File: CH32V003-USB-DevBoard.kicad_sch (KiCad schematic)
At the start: 23 parts, among them J1 USB_C_Receptacle_USB2.0, J2 Conn_01x10, J3 Conn_01x10, J4 Conn_01x01, SW1 SW_Push, U1 ME6211A33M3G-N, U3 CH32V003F4U6, Y1 24MHz

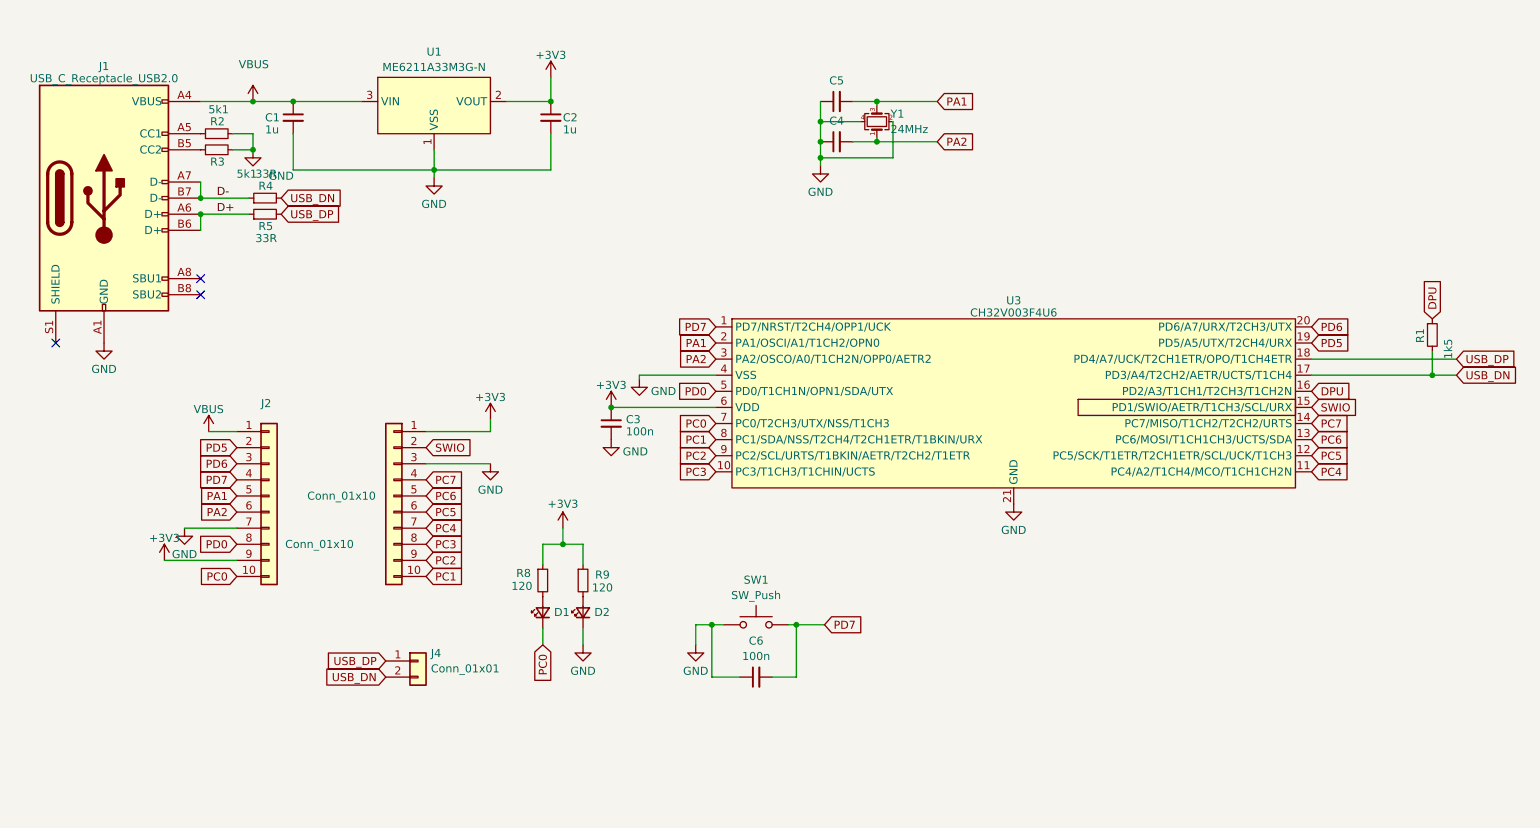
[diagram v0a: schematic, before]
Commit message: Make design easier to hand solder Switch to ch340n instead of S/W bit banged USB
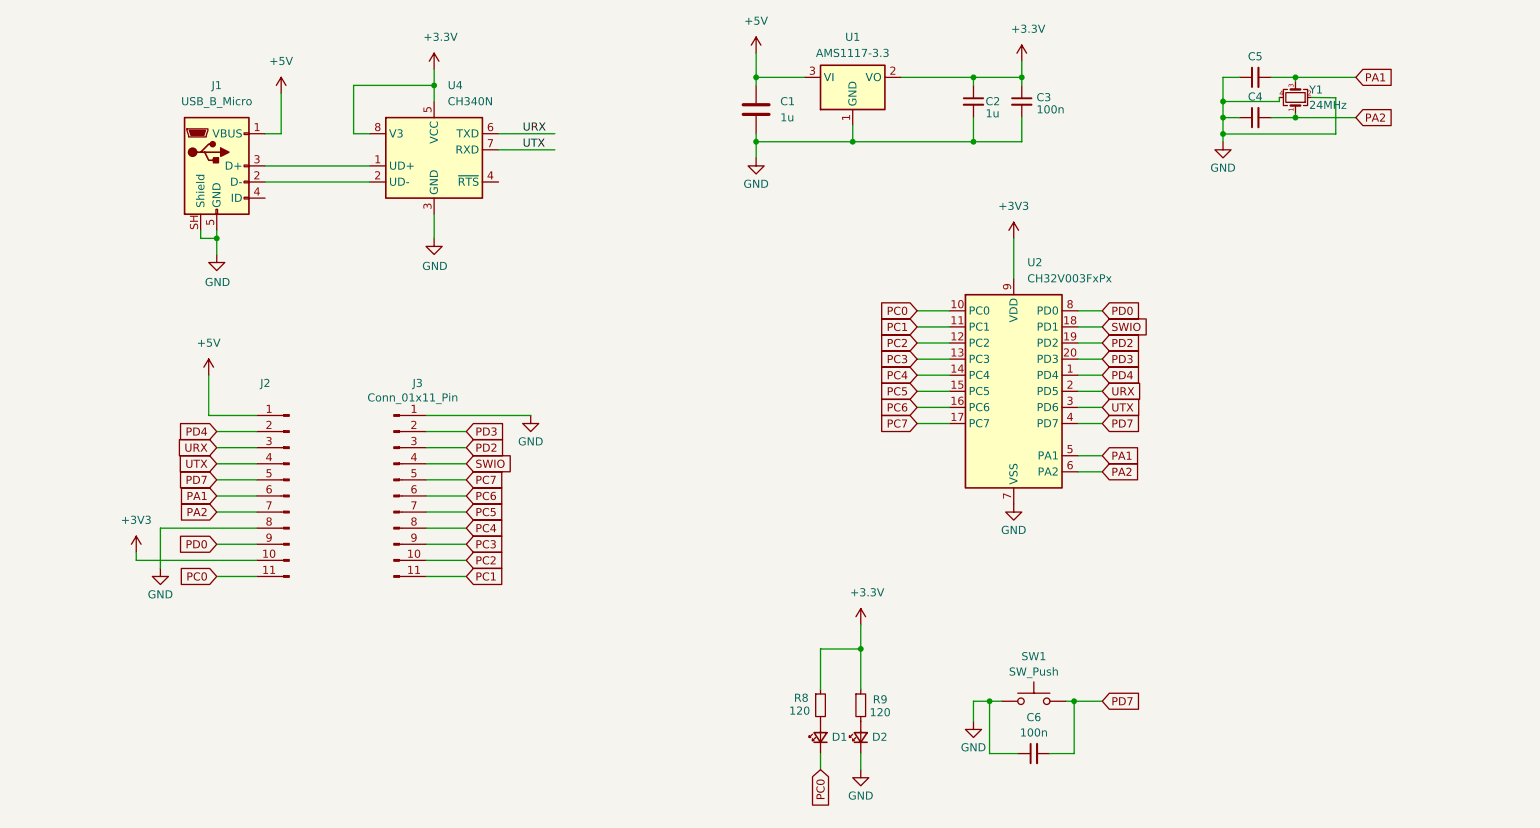
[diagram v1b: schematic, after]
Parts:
- removed C1: 1u, Capacitor_SMD:C_0402_1005Metric, symbol Device:C_Small
- removed J1: USB_C_Receptacle_USB2.0, Connector_USB:USB_C_Receptacle_HRO_TYPE-C-31-M-12, symbol Connector:USB_C_Receptacle_USB2.0
- removed J2, J3: Conn_01x10, Library:PinHeader_1x10_Small, symbol Connector_Generic:Conn_01x10
- removed J4: Conn_01x01, Library:TestPoint_01x02, symbol Connector_Generic:Conn_01x02
- removed R1: 1k5, Resistor_SMD:R_0402_1005Metric, symbol Device:R_Small
- removed R2, R3: 5k1, Resistor_SMD:R_0402_1005Metric, symbol Device:R_Small
- removed R4, R5: 33R, Resistor_SMD:R_0402_1005Metric, symbol Device:R_Small
- removed U1: ME6211A33M3G-N, Package_TO_SOT_SMD:SOT-23-3, symbol WCH:ME6211A33M3G-N
- removed U3: CH32V003F4U6, Package_SO:ETSSOP-20-1EP_4.4x6.5mm_P0.65mm_EP3x4.2mm, symbol CH32V003F4U6:CH32V003F4U6
- added C1: 1u, Capacitor_SMD:C_0603_1608Metric_Pad1.08x0.95mm_HandSolder, symbol Device:C
- added J1: USB_B_Micro, Connector_USB:USB_Micro-B_Amphenol_10118193-0001LF_Horizontal, symbol Connector:USB_B_Micro
- added J2, J3: Conn_01x11_Pin, Connector_PinHeader_2.54mm:PinHeader_1x11_P2.54mm_Vertical, symbol Connector:Conn_01x11_Pin
- added U1: AMS1117-3.3, Package_TO_SOT_SMD:SOT-223-3_TabPin2, symbol Regulator_Linear:AMS1117-3.3
- added U2: CH32V003FxPx, Package_SO:TSSOP-20_4.4x6.5mm_P0.65mm, symbol MCU_WCH_RiscV:CH32V003FxPx
- added U4: CH340N, Package_SO:JEITA_SOIC-8_3.9x4.9mm_P1.27mm, symbol Interface_USB:CH340N
- C2, C3, C4, C5, C6: footprint Capacitor_SMD:C_0402_1005Metric -> Capacitor_SMD:C_0603_1608Metric_Pad1.08x0.95mm_HandSolder
- D1, D2: footprint LED_SMD:LED_0402_1005Metric -> LED_SMD:LED_0603_1608Metric_Pad1.05x0.95mm_HandSolder
- R8: footprint Resistor_SMD:R_0402_1005Metric -> Resistor_SMD:R_0603_1608Metric_Pad0.98x0.95mm_HandSolder
- R9: footprint Resistor_SMD:R_0402_1005Metric -> Capacitor_SMD:C_0603_1608Metric_Pad1.08x0.95mm_HandSolder
- Y1: footprint Crystal:Crystal_SMD_2016-4Pin_2.0x1.6mm -> Crystal:Crystal_SMD_2520-4Pin_2.5x2.0mm
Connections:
- net +3V3: now also J2.10 (Pin_10), U2.9 (VDD); no longer C2.1, C3.1, R8.1, R9.1
- net GND: now also C1.2, J1.5 (GND), J1.SH (Shield), J2.8 (Pin_8), J3.1 (Pin_1), U1.1 (GND), U2.7 (VSS), U4.3 (GND)
- net PA1: now also J2.6 (Pin_6), U2.5 (PA1)
- net PA2: now also J2.7 (Pin_7), U2.6 (PA2)
- net PC0: now also J2.11 (Pin_11), U2.10 (PC0)
- net PC1: now also J3.11 (Pin_11), U2.11 (PC1)
- net PC2: now also J3.10 (Pin_10), U2.12 (PC2)
- net PC3: now also J3.9 (Pin_9), U2.13 (PC3)
- net PC4: now also J3.8 (Pin_8), U2.14 (PC4)
- net PC5: now also J3.7 (Pin_7), U2.15 (PC5)
- net PC6: now also J3.6 (Pin_6), U2.16 (PC6)
- net PC7: now also J3.5 (Pin_5), U2.17 (PC7)
- net PD0: now also J2.9 (Pin_9), U2.8 (PD0)
- net PD7: now also J2.5 (Pin_5), U2.4 (PD7)
- net SWIO: now also J3.4 (Pin_4), U2.18 (PD1)
- new net: J1.2 (D-), U4.2 (UD-)
- new net: J1.3 (D+), U4.1 (UD+)
- new net +3.3V: C2.1, C3.1, R8.1, R9.1, U1.2 (VO), U4.5 (VCC), U4.8 (V3)
- new net +5V: C1.1, J1.1 (VBUS), J2.1 (Pin_1), U1.3 (VI)
- new net PD2: J3.3 (Pin_3), U2.19 (PD2)
- new net PD3: J3.2 (Pin_2), U2.20 (PD3)
- new net PD4: J2.2 (Pin_2), U2.1 (PD4)
- new net URX: J2.3 (Pin_3), U2.2 (PD5), U4.6 (TXD)
- new net UTX: J2.4 (Pin_4), U2.3 (PD6), U4.7 (RXD)
- no-connect marks 3 -> 0
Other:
- moved on the sheet: C2, C4, C5, C6, D1, D2, R8, R9, SW1, Y1
